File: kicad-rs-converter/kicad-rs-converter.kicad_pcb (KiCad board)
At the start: 2 copper layers, 70 x 50 mm, 29 parts

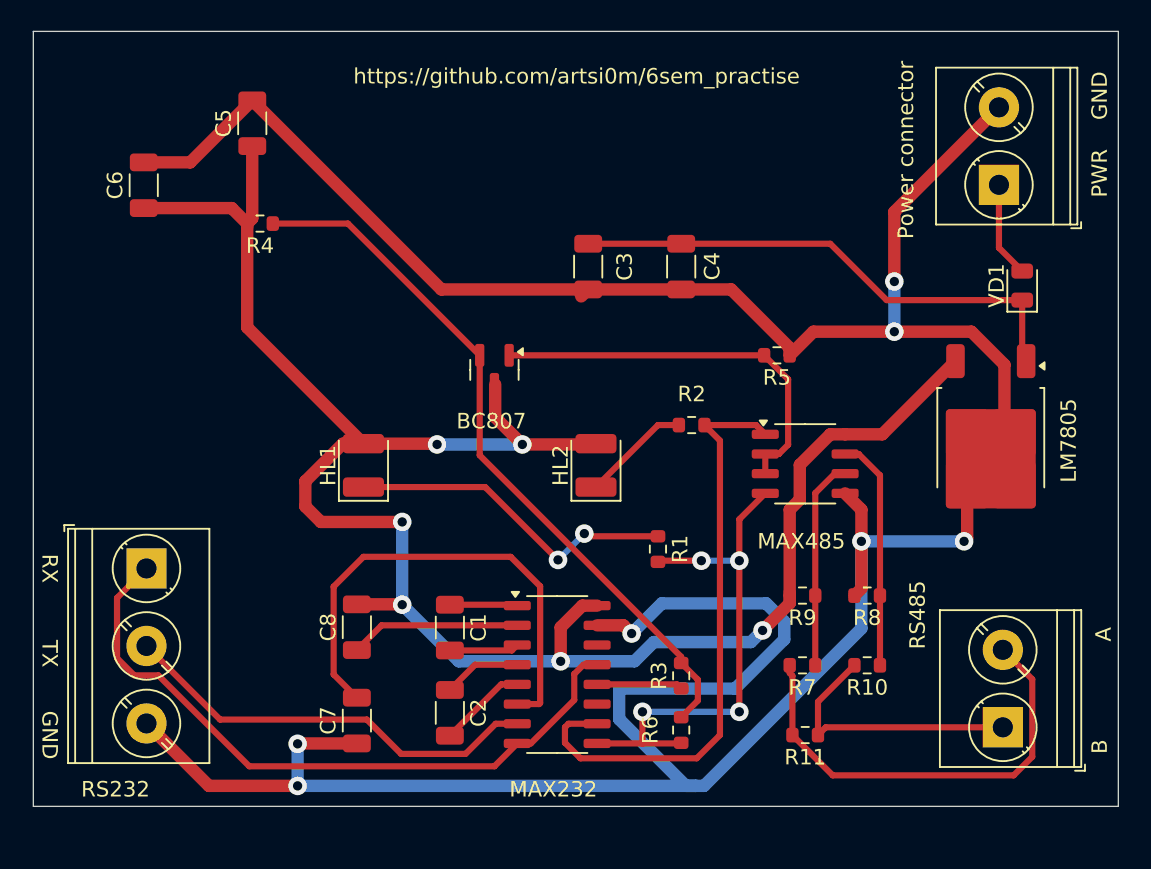
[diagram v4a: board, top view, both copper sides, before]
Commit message: Made PCB layout on 70x40mm board
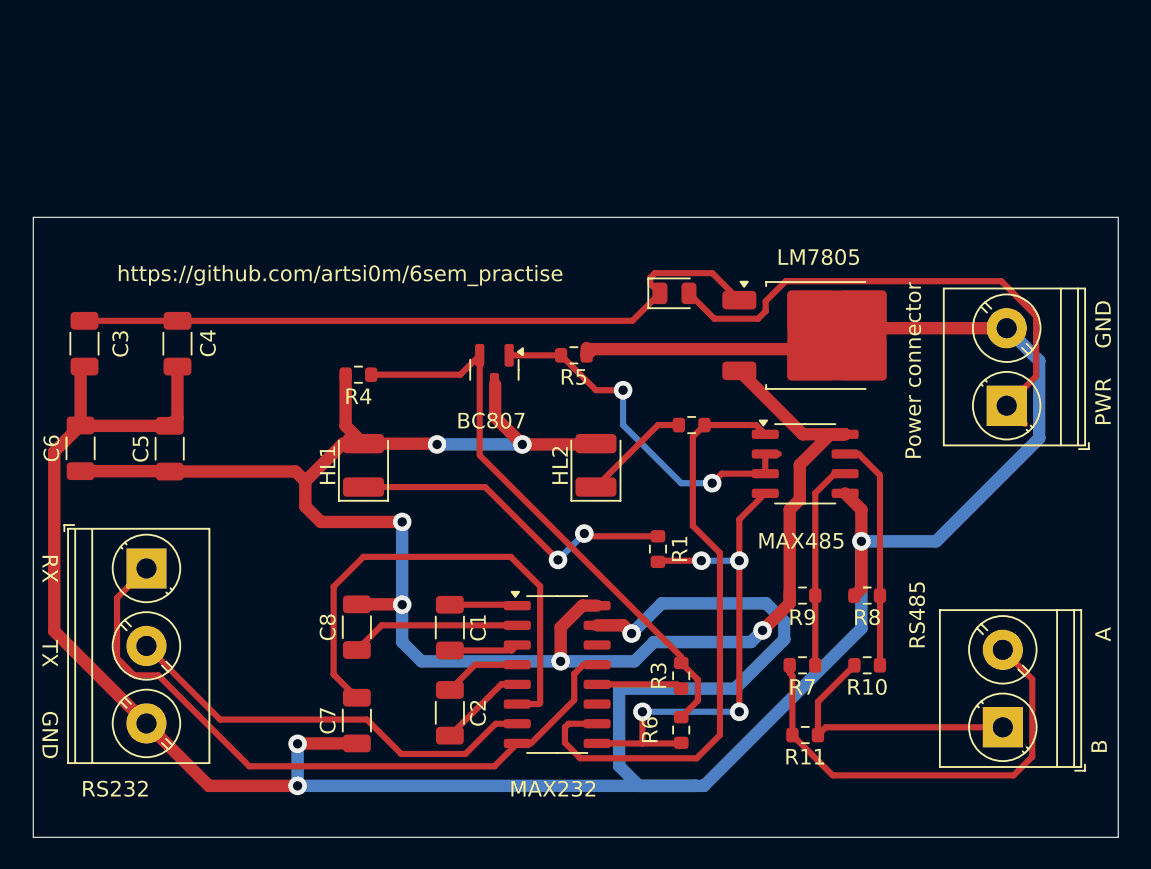
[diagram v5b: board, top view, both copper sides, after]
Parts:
- moved C3 32.9 mm to (128.5, 105.8)
- moved C4 32.9 mm to (134.5, 105.8)
- moved VD1 22.4 mm to (166.6, 102.5), turned to 0 degrees
- moved C5 21.7 mm to (134.0, 112.5)
- moved C6 17.5 mm to (128.2, 112.5)
- moved Power connector 14.3 mm to (188.0, 109.8)
- moved R5 13.1 mm to (160.1, 106.5)
- moved LM7805 13.0 mm to (175.8, 105.2), turned to 0 degrees
- moved R4 11.6 mm to (146.2, 107.8)
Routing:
- net Net-(VD1-A): track 6.18 -> 33.6 mm
- net GND: track 208.9 -> 192.0 mm, vias 7 -> 4
- net Net-(DA2-VI): track 33.5 -> 45.7 mm
- net Net-(VT1-E): track 46.5 -> 37.1 mm
- net +5V: track 125.7 -> 116.7 mm
- net Net-(DA3-DE): track 25.9 -> 23.7 mm, vias 0 -> 2
- net Net-(DA1-TXIN2): track 38.8 -> 39.4 mm
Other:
- board size 70 x 50 mm -> 70 x 40 mm

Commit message: Moved transistor BC807 and redone PCB layout a little bit.
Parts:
- moved BC807 13.0 mm to (161.0, 119.0)
- moved R4 11.3 mm to (153.0, 116.8)
- moved HL2 3.26 mm to (158.2, 113.8), turned to -90 degrees
- moved R1 2.70 mm to (167.8, 117.5), turned to 0 degrees
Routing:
- net +5V: track 116.7 -> 105.9 mm, vias 6 -> 4
- net Net-(VT1-E): track 37.1 -> 28.1 mm
- net Net-(DA3-DE): track 23.7 -> 31.1 mm, vias 2 -> 3
- net Net-(DA1-TXIN2): track 39.4 -> 42.2 mm, vias 0 -> 2
- net Net-(DA1-~{RXOUT2}): track 33.8 -> 31.3 mm, vias 4 -> 2
- net Net-(HL2-K): track 7.01 -> 9.20 mm
- net Net-(HL1-K): track 21.7 -> 22.4 mm, vias 2 -> 0

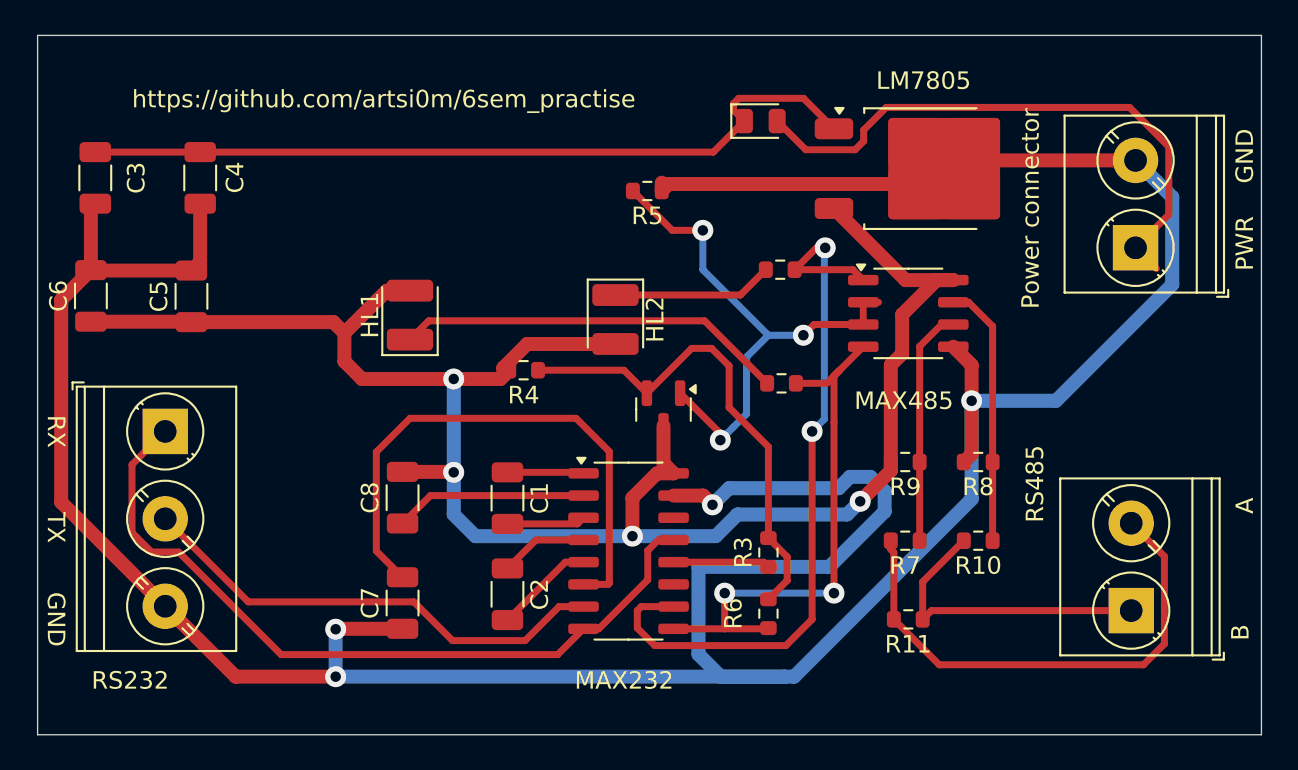
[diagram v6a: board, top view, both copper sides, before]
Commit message: Rebuild from scratch. 0.8 track_width and 60x40mm board
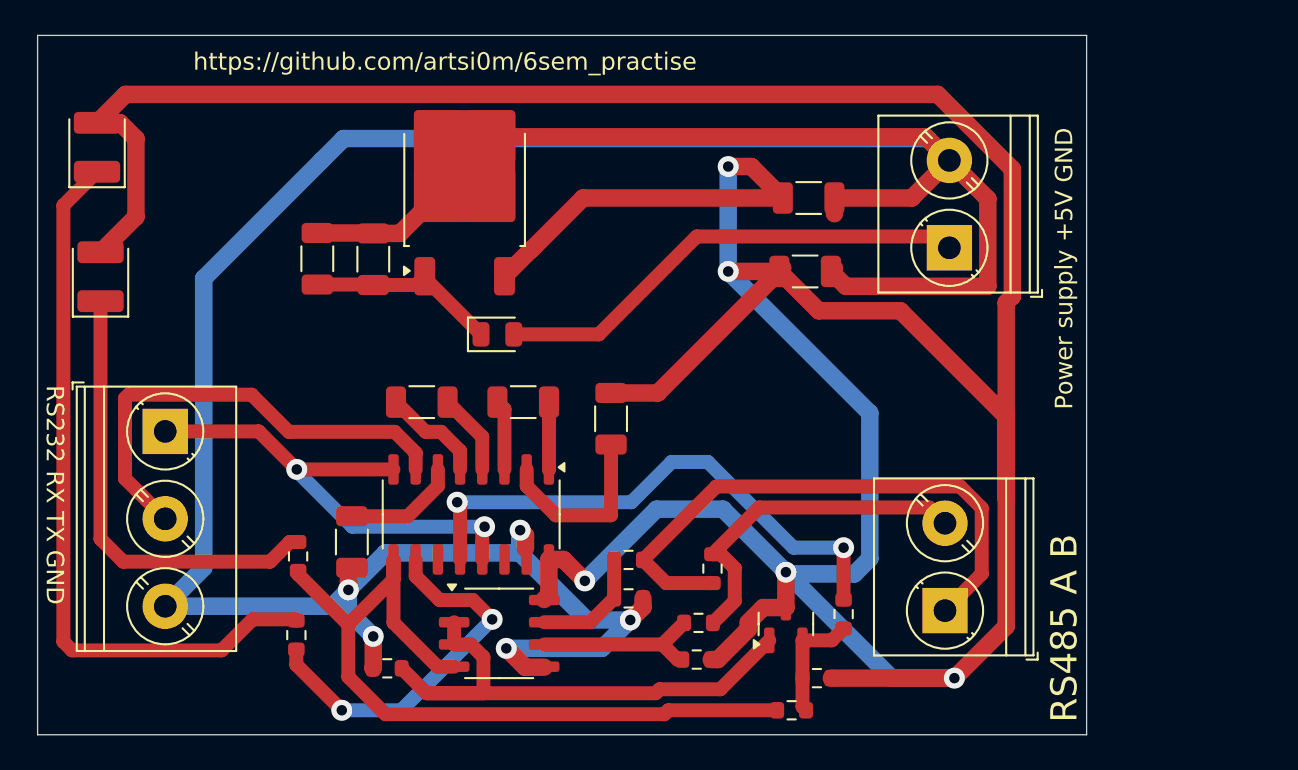
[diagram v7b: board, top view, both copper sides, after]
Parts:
- X1: renamed from Power connector
- moved C6 40.9 mm to (169.1, 111.1), turned to 0 degrees
- moved C5 35.7 mm to (169.3, 106.9), turned to 0 degrees
- moved R2 34.7 mm to (140.0, 131.9), turned to -90 degrees
- moved HL2 31.2 mm to (128.6, 104.0), turned to 90 degrees
- moved R5 31.1 mm to (145.2, 133.8), turned to 0 degrees
- moved DA3 29.7 mm to (151.6, 131.8)
- moved R1 29.4 mm to (140.1, 127.4), turned to -90 degrees
- moved DA2 26.2 mm to (149.6, 106.3), turned to 90 degrees
- moved R4 24.3 mm to (169.8, 134.4), turned to 0 degrees
- moved R8 21.5 mm to (159.0, 129.8), turned to 0 degrees
- moved R10 20.0 mm to (159.0, 127.6), turned to 0 degrees
- moved VD1 19.4 mm to (151.5, 114.7)
- moved HL1 17.8 mm to (128.8, 111.4)
- moved C3 16.6 mm to (144.4, 110.4), turned to 90 degrees
- moved R9 16.4 mm to (162.9, 133.3), turned to 0 degrees
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- renumbered MAX232 to DA1, LM7805 to DA2, MAX485 to DA3, BC807 to VT1, RS232 to X2, RS485 to X3
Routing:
- net +5V: track 105.9 -> 231.2 mm, vias 4 -> 5
- net Net-(DA2-VI): track 45.7 -> 11.0 mm
- net Net-(HL2-K): track 9.20 -> 42.0 mm
- net Net-(DA1-~{RXOUT1}): track 5.54 -> 31.4 mm, vias 0 -> 2
- net Net-(DA1-V-): track 31.7 -> 6.59 mm
- net Net-(VT1-E): track 28.1 -> 6.71 mm
- net Net-(DA1-TXIN2): track 42.2 -> 21.7 mm
- net Net-(DA1-RXIN1): track 44.1 -> 28.0 mm, vias 0 -> 2
- net Net-(R10-Pad2): track 17.6 -> 32.9 mm
- net Net-(DA1-~{RXOUT2}): track 31.3 -> 45.7 mm, vias 2 -> 0
- net GND: track 191.7 -> 178.8 mm, vias 4 -> 5
- net Net-(R11-Pad2): track 29.3 -> 20.0 mm
- net Net-(DA3-BZ): track 15.1 -> 6.77 mm
- net Net-(VD1-A): track 33.6 -> 27.5 mm
- net Net-(HL1-K): track 22.4 -> 26.2 mm
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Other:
- board size 70 x 40 mm -> 60 x 40 mm
- board text added: "Power supply +5V GND"
- board text added: "RS232 RX TX GND"
- board text added: "RS485 A B"
- board text removed: "A"
- board text removed: "B"
- board text removed: "GND"
- board text removed: "PWR"
- board text removed: "RX"
- board text removed: "TX"

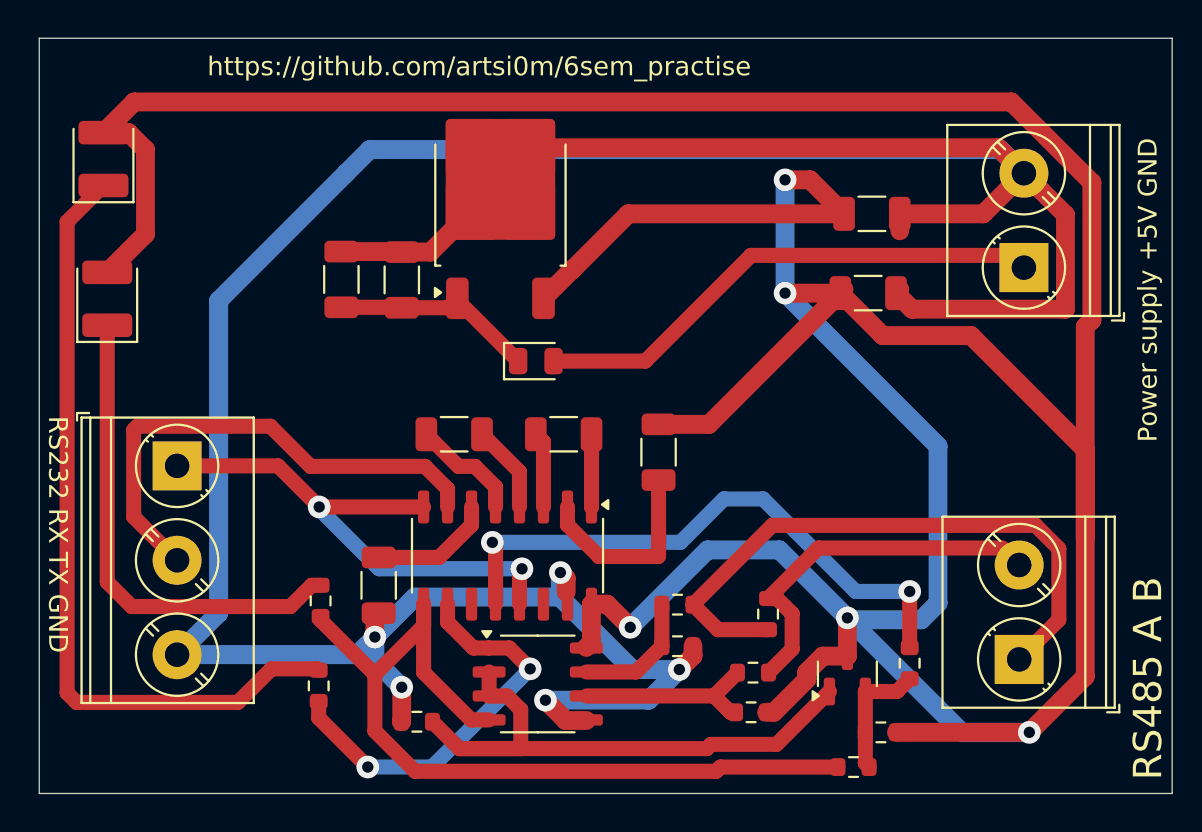
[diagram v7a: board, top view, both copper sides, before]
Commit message: Silkscreen added on pcb
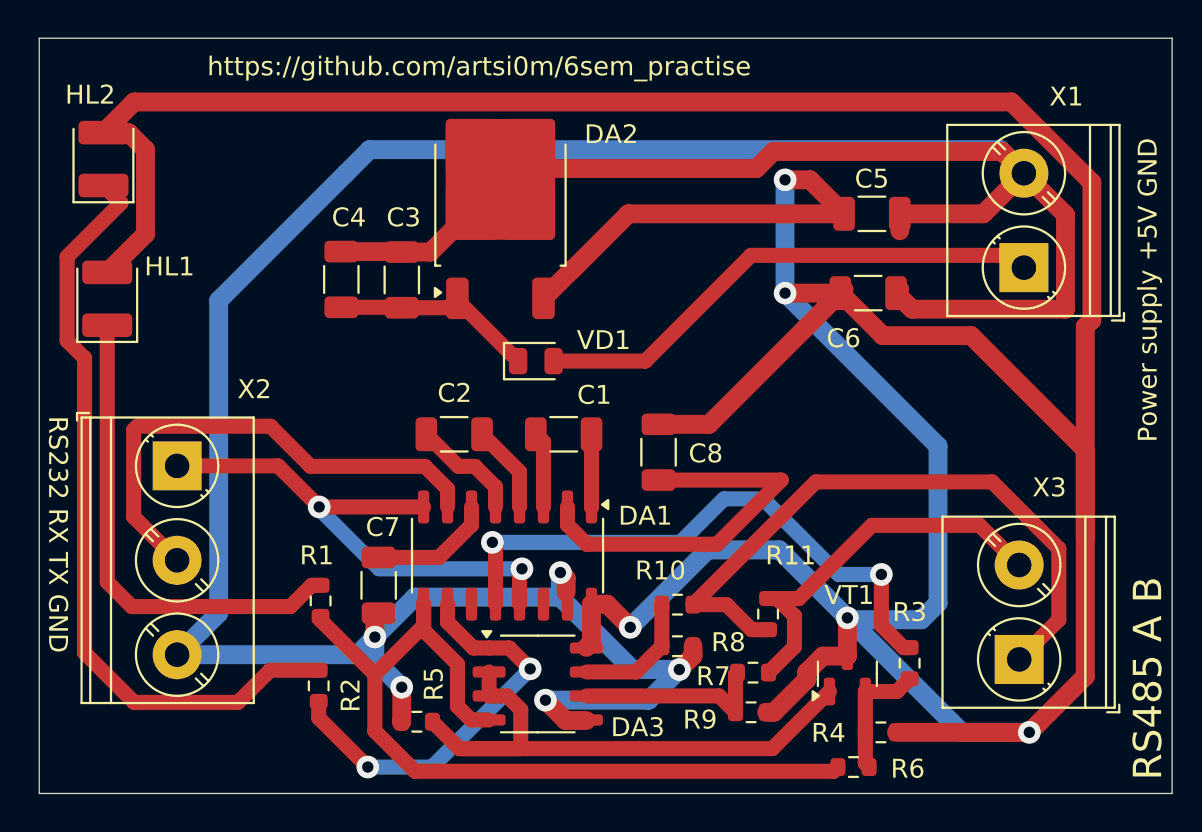
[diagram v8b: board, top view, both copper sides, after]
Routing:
- net Net-(DA1-V+): track 10.5 -> 20.6 mm
- net Net-(R10-Pad2): track 32.9 -> 34.8 mm
- net Net-(R11-Pad2): track 20.0 -> 21.1 mm
- net Net-(HL2-K): track 42.0 -> 40.9 mm
